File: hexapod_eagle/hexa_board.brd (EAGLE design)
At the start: 80 x 90 mm, 38 parts

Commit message: Hexapod board v2
Changelog:
-new package for voltage regulator
-supply for ground sensor
-fix voltage sensor
-second battery voltage sensor
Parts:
- removed 3V3, 5V5: LM1117MP-3.3, lm1117_10:SOT223
- added 3V, 5V: MC33269, mc33269:TO220
- added BATERIA_2: (no value), con-ptr500:AK300/2
- added R10, R11: 510r, rcl:R0805
- added R4, R5, R6, R7, R8, R9: 10k, rcl:R0805
- added WLACZNIK: (no value), switch:255SB
- CZUJNIK_PODLOZA: device pinhead:1X06 -> pinhead:2X06
- moved C1 41.3 mm to (33.3, -34.0), flipped to the top
- moved C2 38.5 mm to (33.3, -31.1), flipped to the top
- moved C3 35.4 mm to (35.7, -12.9), turned to 180 degrees
- moved C4 35.1 mm to (35.7, -16.8), turned to 180 degrees
- moved C7 28.1 mm to (25.0, 36.0)
- moved C9 27.6 mm to (25.0, 32.0)
- moved R2 6.09 mm to (-11.2, -31.6), turned to 270 degrees
- moved R1 1.94 mm to (-7.50, -34.3)
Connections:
- new net BATTERY2: R10.1, R11.2, TEENSY41.22/A8
- new net BAT_IN: BATERIA.1, WLACZNIK.1
- new net BAT_IN2: BATERIA_2.1, R10.2
- new net N$1: CZUJNIK_PODLOZA.2, R4.2
- new net N$2: CZUJNIK_PODLOZA.4, R5.2
- new net N$3: CZUJNIK_PODLOZA.6, R6.2
- new net N$5: CZUJNIK_PODLOZA.8, R7.2
- new net N$6: CZUJNIK_PODLOZA.10, R8.2
- new net N$7: CZUJNIK_PODLOZA.12, R9.2
- net +3V3: now also 3V.1; no longer 3V3.2, 3V3.4
- net +5V: now also 5V.1; no longer 5V5.2, 5V5.4, R1.2
- net +6V2: no longer 3V3.3, C7.+, C9.+
- net +BAT: now also 3V.3, 5V.3, C7.+, C9.+, R1.2, WLACZNIK.2; no longer 5V5.3, BATERIA.1
- net GND: now also 3V.2, 5V.2, BATERIA_2.2, R11.1, R4.1, R5.1, R6.1, R7.1, R8.1, R9.1; no longer 3V3.1, 5V5.1
- net LEG1: now also TEENSY41.21/A7; no longer TEENSY41.22/A8
- net LEG2: now also CZUJNIK_PODLOZA.3, TEENSY41.20/A6; no longer CZUJNIK_PODLOZA.2, TEENSY41.21/A7
- net LEG3: now also CZUJNIK_PODLOZA.5, TEENSY41.17/A3; no longer CZUJNIK_PODLOZA.3, TEENSY41.20/A6
- net LEG4: now also CZUJNIK_PODLOZA.7; no longer CZUJNIK_PODLOZA.4
- net LEG5: now also CZUJNIK_PODLOZA.9; no longer CZUJNIK_PODLOZA.5
- net LEG6: now also CZUJNIK_PODLOZA.11; no longer CZUJNIK_PODLOZA.6
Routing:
- net +BAT: track 34.4 -> 161.2 mm, vias 1 -> 0
- net +6V2: track 129.2 -> 95.6 mm
- net +3V3: track 115.9 -> 138.7 mm, vias 2 -> 4
- net BATTERY2: track 0.00 -> 19.8 mm
- net +5V: track 95.0 -> 107.9 mm
- net BAT_IN2: track 0.00 -> 9.75 mm
- net LEG3: track 23.8 -> 30.3 mm
- net BAT_IN: track 0.00 -> 6.28 mm
- net N$7: track 0.00 -> 5.46 mm
- net N$6: track 0.00 -> 5.27 mm
- net N$5: track 0.00 -> 5.08 mm
- net N$1: track 0.00 -> 5.05 mm
- net N$3: track 0.00 -> 4.89 mm
- net N$2: track 0.00 -> 4.86 mm
- net BATTERY: track 23.4 -> 18.7 mm
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
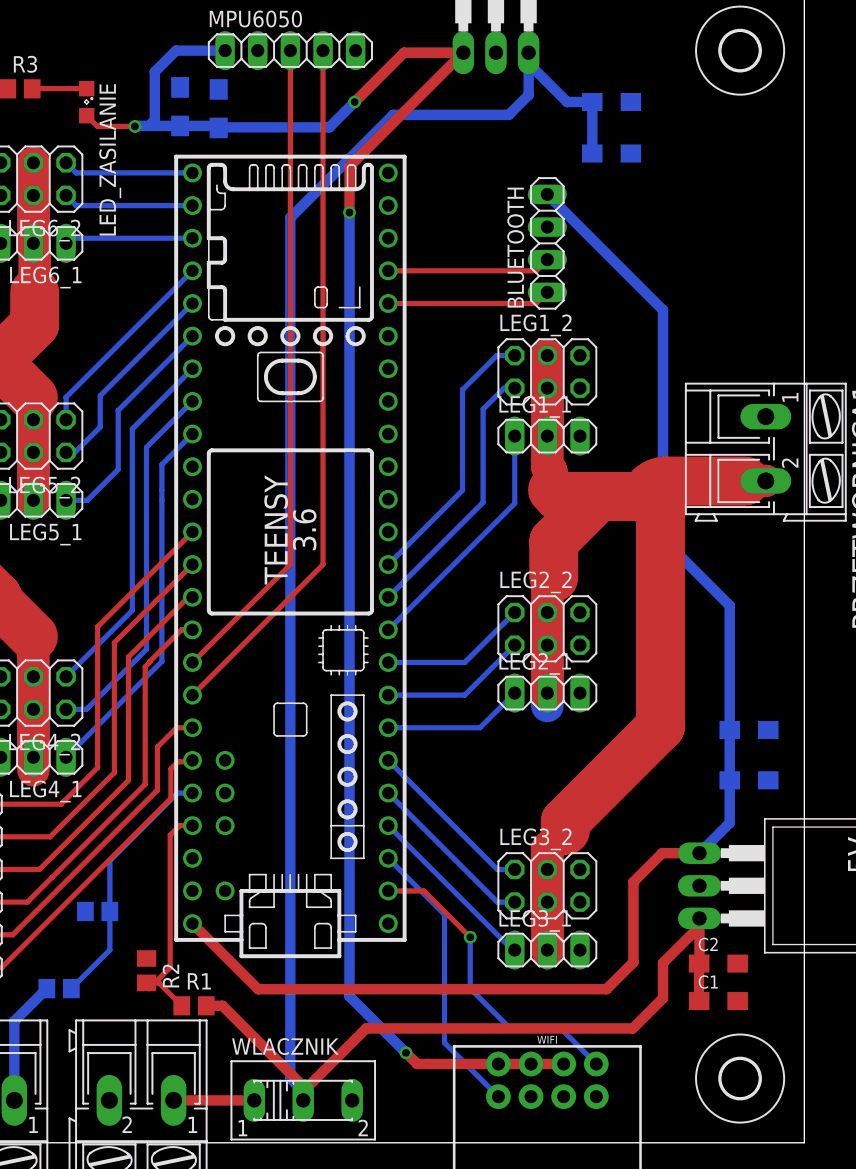
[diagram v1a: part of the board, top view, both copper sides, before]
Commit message: Board v2
Changelog:
-on/off swich for power mcu(was in last update)
-add 2 leds for comunication
-some positions changes
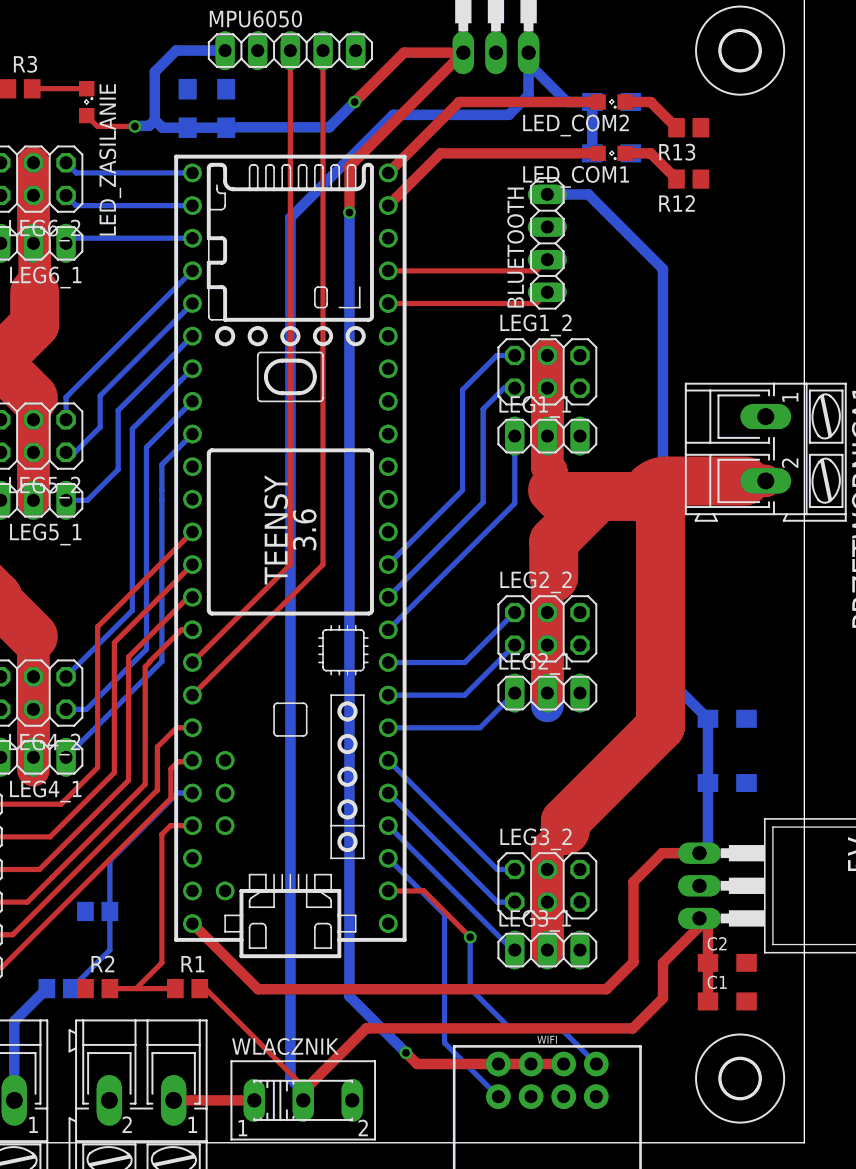
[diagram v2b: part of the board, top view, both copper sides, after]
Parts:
- added LED_COM1, LED_COM2: (no value), led:SML0805
- added R12, R13: 510r, rcl:R0805
- moved R2 4.06 mm to (-15.0, -33.0), turned to 0 degrees
- moved C3 1.90 mm to (34.0, -12.0)
- moved C4 1.70 mm to (34.0, -17.0)
- moved R1 1.43 mm to (-8.00, -33.0)
- moved C2 0.69 mm to (34.0, -31.0)
- moved C1 0.69 mm to (34.0, -34.0)
- moved C10 0.60 mm to (-8.00, 35.5)
- moved C8 0.58 mm to (-5.00, 35.5)
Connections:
- new net LED1: LED_COM1.A, TEENSY41.31/A12
- new net LED2: LED_COM2.A, TEENSY41.32/A13
- new net N$8: LED_COM1.C, R12.2
- new net N$9: LED_COM2.C, R13.2
- net GND: now also R12.1, R13.1
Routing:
- net LED2: track 0.00 -> 18.6 mm
- net LED1: track 0.00 -> 18.0 mm
- net N$9: track 0.00 -> 4.83 mm
- net N$8: track 0.00 -> 4.83 mm
- net BATTERY: track 18.7 -> 20.6 mm
- net +BAT: track 161.2 -> 162.5 mm

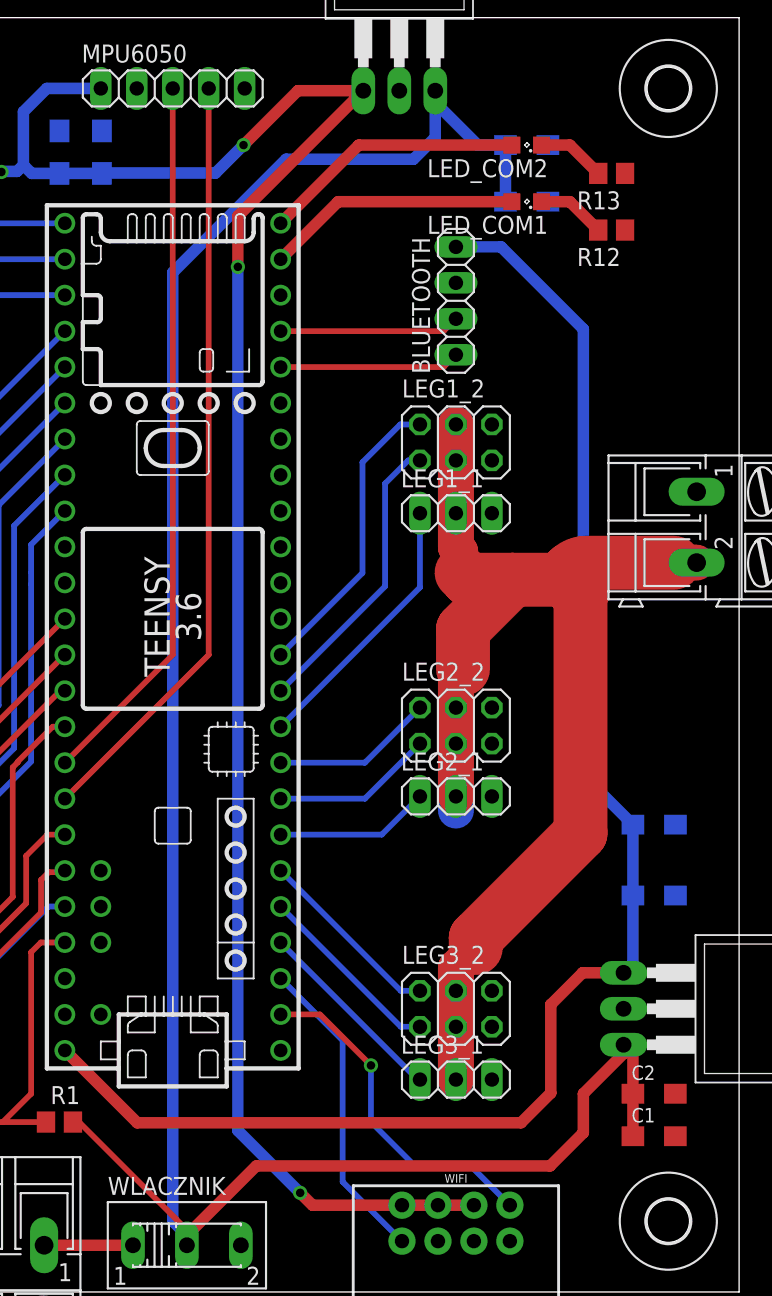
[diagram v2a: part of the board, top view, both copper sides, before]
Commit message: Update board project
-fix voltage regulator output
-added tantalum capacitors (B size)instead cpol
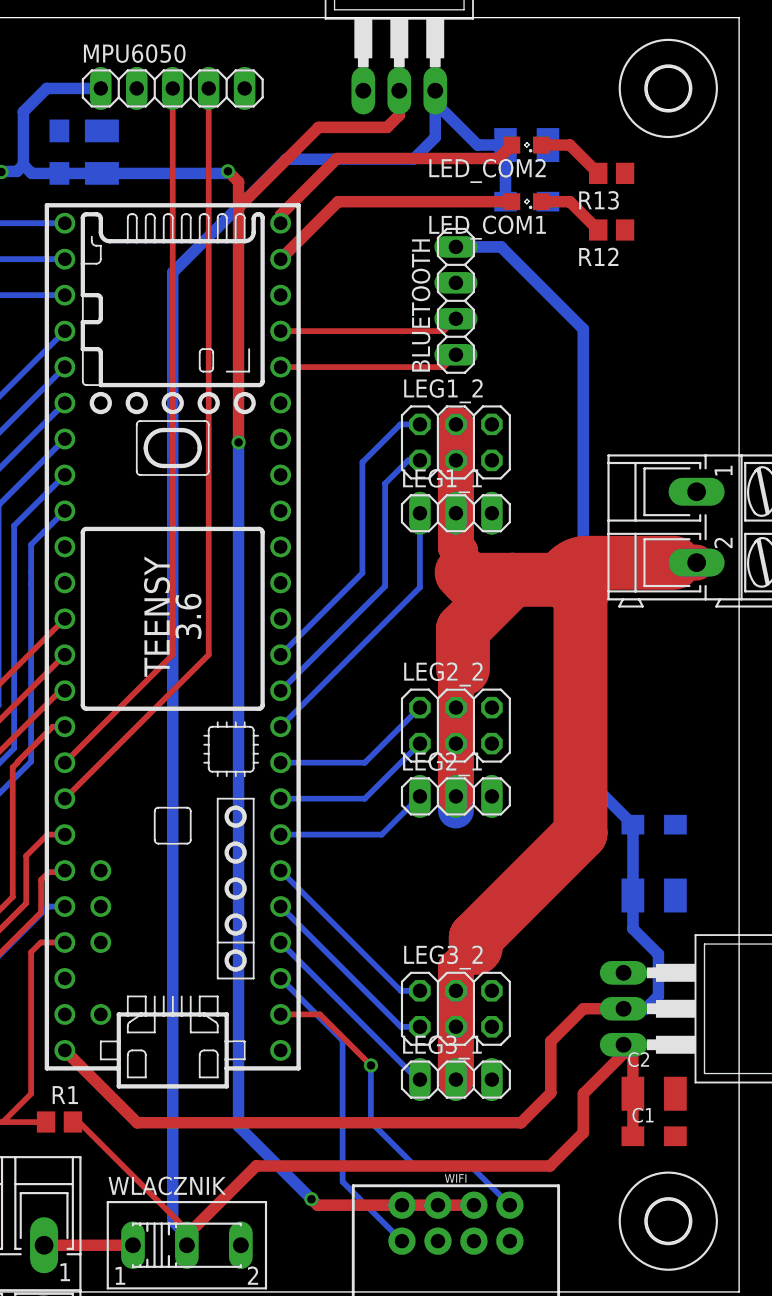
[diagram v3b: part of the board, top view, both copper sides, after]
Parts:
- C2, C3, C7, C8: device rcl:SMC_A -> rcl:SMC_B
- moved C3 5.00 mm to (34.0, -17.0)
- moved C4 5.00 mm to (34.0, -12.0)
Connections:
- net +3V3: now also 3V.2; no longer 3V.1
- net +5V: now also 5V.2; no longer 5V.1
- net GND: now also 3V.1, 5V.1; no longer 3V.2, 5V.2
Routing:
- net +3V3: track 138.9 -> 133.0 mm
- net +5V: track 108.2 -> 110.6 mm
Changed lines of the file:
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@@
 <layer number="14" name="Route14" color="1" fill="6" visible="no" active="no"/>
 <layer number="15" name="Route15" color="4" fill="6" visible="no" active="no"/>
-<layer number="16" name="Bottom" color="1" fill="1" visible="no" active="yes"/>
+<layer number="16" name="Bottom" color="1" fill="1" visible="yes" active="yes"/>
 <layer number="17" name="Pads" color="2" fill="1" visible="yes" active="yes"/>
 <layer number="18" name="Vias" color="2" fill="1" visible="yes" active="yes"/>
@@
 <elements>
 <element name="C10" library="rcl" package="SMC_A" value="100n" x="-8" y="35.5" rot="MR90"/>
-<element name="C7" library="rcl" package="SMC_A" value="10uF" x="25" y="36" rot="MR180"/>
-<element name="C8" library="rcl" package="SMC_A" value="10uF" x="-5" y="35.5" rot="MR90"/>
+<element name="C7" library="rcl" package="SMC_B" value="10uF" x="25" y="36" rot="MR180"/>
+<element name="C8" library="rcl" package="SMC_B" value="10uF" x="-5" y="35.5" rot="MR90"/>
 <element name="C9" library="rcl" package="SMC_A" value="100n" x="25" y="32" rot="MR180"/>
 <element name="LED_ZASILANIE" library="led" package="SML0805" value="" x="-15.85" y="35.99" rot="R270"/>
@@
 <element name="TEENSY41" library="teensy" package="TEENSY_3.5/3.6_BASIC" value="TEENSY_3.5/3.6_BASIC" x="0" y="0" rot="R90"/>
 <element name="C1" library="rcl" package="SMC_A" value="100n" x="34" y="-34"/>
-<element name="C2" library="rcl" package="SMC_A" value="10uF" x="34" y="-31"/>
-<element name="C3" library="rcl" package="SMC_A" value="10uF" x="34" y="-12" rot="MR180"/>
-<element name="C4" library="rcl" package="SMC_A" value="100n" x="34" y="-17" rot="MR180"/>
+<element name="C2" library="rcl" package="SMC_B" value="10uF" x="34" y="-31"/>
+<element name="C3" library="rcl" package="SMC_B" value="10uF" x="34" y="-17" rot="MR180"/>
+<element name="C4" library="rcl" package="SMC_A" value="100n" x="34" y="-12" rot="MR180"/>
 <element name="WIFI" library="SparkFun-RF" package="ESP8266_ESP-01" value="ESP8266_ESP-01" x="20" y="-50" rot="R180">
 <attribute name="SF_ID" value="WRL-13678" x="20" y="-50" size="1.778" layer="27" rot="R180" display="off"/>
@@
 <wire x1="-12.1" y1="34.1" x2="-15.01" y2="34.1" width="0.4064" layer="1"/>
 <wire x1="-15.01" y1="34.1" x2="-15.85" y2="34.94" width="0.4064" layer="1"/>
-<contactref element="3V" pad="1"/>
-<wire x1="13.46" y1="39.84" x2="4.6" y2="30.98" width="0.8128" layer="1"/>
-<wire x1="4.6" y1="30.98" x2="4.6" y2="27.4" width="0.8128" layer="1"/>
-<via x="4.6" y="27.4" extent="1-16" drill="0.6" shape="square"/>
-<wire x1="4.6" y1="27.4" x2="4.6" y2="-33.6" width="0.8128" layer="16"/>
-<wire x1="4.6" y1="-33.6" x2="9" y2="-38" width="0.8128" layer="16"/>
-<via x="9" y="-38" extent="1-16" drill="0.6" shape="square"/>
-<wire x1="9" y1="-38" x2="9.87" y2="-38.87" width="0.8128" layer="1"/>
-<wire x1="9.87" y1="-38.87" x2="16.19" y2="-38.87" width="0.8128" layer="1"/>
 <wire x1="18.73" y1="-38.87" x2="16.19" y2="-38.87" width="0.8128" layer="1"/>
 <wire x1="21.27" y1="-38.87" x2="18.73" y2="-38.87" width="0.8128" layer="1"/>
-<via x="5" y="36" extent="1-16" drill="0.6" shape="square"/>
-<wire x1="5" y1="36" x2="8.84" y2="39.84" width="0.8128" layer="1"/>
-<wire x1="8.84" y1="39.84" x2="13.46" y2="39.84" width="0.8128" layer="1"/>
 <wire x1="-11" y1="34.14" x2="-12.06" y2="34.14" width="0.8128" layer="16"/>
 <wire x1="-12.06" y1="34.14" x2="-12.1" y2="34.1" width="0.8128" layer="16"/>
@@
 <wire x1="-10.55" y1="38.35" x2="-10.55" y2="34.59" width="0.8128" layer="16"/>
 <wire x1="-10.55" y1="34.59" x2="-11" y2="34.14" width="0.8128" layer="16"/>
-<wire x1="-5.53" y1="34.03" x2="-5" y2="34.03" width="0.8128" layer="16"/>
-<wire x1="-5" y1="34.03" x2="3.03" y2="34.03" width="0.8128" layer="16"/>
-<wire x1="3.03" y1="34.03" x2="5" y2="36" width="0.8128" layer="16"/>
 <wire x1="-5" y1="34" x2="-8" y2="34" width="0.8128" layer="16"/>
-<wire x1="-5" y1="34" x2="-5" y2="34.03" width="0.8128" layer="16"/>
 <wire x1="-8" y1="34" x2="-9.96" y2="34" width="0.8128" layer="16"/>
 <wire x1="-9.96" y1="34" x2="-10.55" y2="34.59" width="0.8128" layer="16"/>
+<contactref element="3V" pad="2"/>
+<wire x1="16.19" y1="-38.87" x2="10.22" y2="-38.87" width="0.8128" layer="1"/>
+<wire x1="10.22" y1="-38.87" x2="9.8" y2="-38.45" width="0.8128" layer="1"/>
+<via x="9.8" y="-38.45" extent="1-16" drill="0.6" shape="square"/>
+<wire x1="9.8" y1="-38.45" x2="4.65" y2="-33.3" width="0.8128" layer="16"/>
+<wire x1="4.65" y1="-33.3" x2="4.65" y2="15" width="0.8128" layer="16"/>
+<via x="4.65" y="15" extent="1-16" drill="0.6" shape="square"/>
+<wire x1="4.65" y1="15" x2="4.65" y2="31.6" width="0.8128" layer="1"/>
+<wire x1="4.65" y1="31.6" x2="4.65" y2="33.4" width="0.8128" layer="1"/>
+<wire x1="16" y1="39.84" x2="16" y2="38.1" width="0.8128" layer="1"/>
+<wire x1="16" y1="38.1" x2="15.15" y2="37.25" width="0.8128" layer="1"/>
+<wire x1="-5" y1="34" x2="3.75" y2="34" width="0.8128" layer="16"/>
+<wire x1="3.75" y1="34" x2="3.9" y2="34.15" width="0.8128" layer="16"/>
+<via x="3.9" y="34.15" extent="1-16" drill="0.6" shape="square"/>
+<wire x1="3.9" y1="34.15" x2="4.65" y2="33.4" width="0.8128" layer="1"/>
+<wire x1="4.65" y1="31.6" x2="10.3" y2="37.25" width="0.8128" layer="1"/>
+<wire x1="10.3" y1="37.25" x2="15.15" y2="37.25" width="0.8128" layer="1"/>
 </signal>
 <signal name="GND">
@@
 <contactref element="BATERIA_2" pad="2"/>
 <contactref element="R11" pad="1"/>
-<contactref element="5V" pad="2"/>
-<contactref element="3V" pad="2"/>
 <contactref element="R12" pad="1"/>
 <contactref element="R13" pad="1"/>
+<contactref element="3V" pad="1"/>
+<contactref element="5V" pad="1"/>
 </signal>
 <signal name="INT">
@@
 <contactref element="TEENSY41" pad="VIN"/>
 <contactref element="BLUETOOTH" pad="4"/>
-<contactref element="5V" pad="1"/>
-<wire x1="31.84" y1="-22.46" x2="28.94" y2="-22.46" width="0.8128" layer="1"/>
-<wire x1="28.94" y1="-22.46" x2="26.7" y2="-24.7" width="0.8128" layer="1"/>
-<wire x1="26.7" y1="-24.7" x2="26.7" y2="-30.95" width="0.8128" layer="1"/>
 <wire x1="26.7" y1="-30.95" x2="24.6" y2="-33.05" width="0.8128" layer="1"/>
 <wire x1="24.6" y1="-33.05" x2="-2.51" y2="-33.05" width="0.8128" layer="1"/>
 <wire x1="-2.51" y1="-33.05" x2="-7.62" y2="-27.94" width="0.8128" layer="1"/>
 <wire x1="29" y1="-8.5" x2="29" y2="23" width="0.8128" layer="16"/>
-<wire x1="32.5" y1="-17" x2="32.5" y2="-21.8" width="0.8128" layer="16"/>
-<wire x1="32.5" y1="-21.8" x2="31.84" y2="-22.46" width="0.8128" layer="16"/>
-<wire x1="32.5" y1="-17" x2="32.5" y2="-12" width="0.8128" layer="16"/>
-<wire x1="29" y1="-8.5" x2="32.5" y2="-12" width="0.8128" layer="16"/>
 <wire x1="20" y1="28.81" x2="23.19" y2="28.81" width="0.8128" layer="16"/>
 <wire x1="29" y1="23" x2="23.19" y2="28.81" width="0.8128" layer="16"/>
+<contactref element="5V" pad="2"/>
+<wire x1="26.7" y1="-30.95" x2="26.7" y2="-27.3" width="0.8128" layer="1"/>
+<wire x1="26.7" y1="-27.3" x2="29" y2="-25" width="0.8128" layer="1"/>
+<wire x1="31.84" y1="-25" x2="29" y2="-25" width="0.8128" layer="1"/>
+<wire x1="29" y1="-8.5" x2="32.5" y2="-12" width="0.8128" layer="16"/>
+<wire x1="32.5" y1="-12" x2="32.5" y2="-17" width="0.8128" layer="16"/>
+<wire x1="31.84" y1="-25" x2="33.4" y2="-25" width="0.8128" layer="16"/>
+<wire x1="33.4" y1="-25" x2="33.7" y2="-24.7" width="0.8128" layer="16"/>
+<wire x1="33.7" y1="-24.7" x2="34.05" y2="-24.35" width="0.8128" layer="16"/>
+<wire x1="32.5" y1="-17" x2="32.5" y2="-19.35" width="0.8128" layer="16"/>
+<wire x1="32.5" y1="-19.35" x2="34.3" y2="-21.15" width="0.8128" layer="16"/>
+<wire x1="34.3" y1="-21.15" x2="34.3" y2="-24.1" width="0.8128" layer="16"/>
+<wire x1="34.3" y1="-24.1" x2="34.05" y2="-24.35" width="0.8128" layer="16"/>
 </signal>
 <signal name="RXD">
@@
 <contactref element="LED_COM2" pad="A"/>
 <contactref element="TEENSY41" pad="32/A13"/>
-<wire x1="23.95" y1="36" x2="13.14" y2="36" width="0.8128" layer="1"/>
-<wire x1="13.14" y1="36" x2="7.62" y2="30.48" width="0.8128" layer="1"/>
+<wire x1="7.62" y1="30.48" x2="7.62" y2="31.07" width="0.8128" layer="1"/>
+<wire x1="7.62" y1="31.07" x2="11.6" y2="35.05" width="0.8128" layer="1"/>
+<wire x1="11.6" y1="35.05" x2="23" y2="35.05" width="0.8128" layer="1"/>
+<wire x1="23" y1="35.05" x2="23.95" y2="36" width="0.8128" layer="1"/>
 </signal>
 </signals>
